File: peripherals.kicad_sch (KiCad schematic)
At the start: 81 parts, among them J10 533980471, J11 ERF8-040-05.0-L-DV-K-TR, J7 Conn_02x08_Counter_Clockwise, J9 TC2050-IDC-NL, Q10 PJE138K, Q9 PJE138K, U30 TPD4E05U06QDQARQ1, U33 NTS0102GT, U34 PCAL6408ABSHP

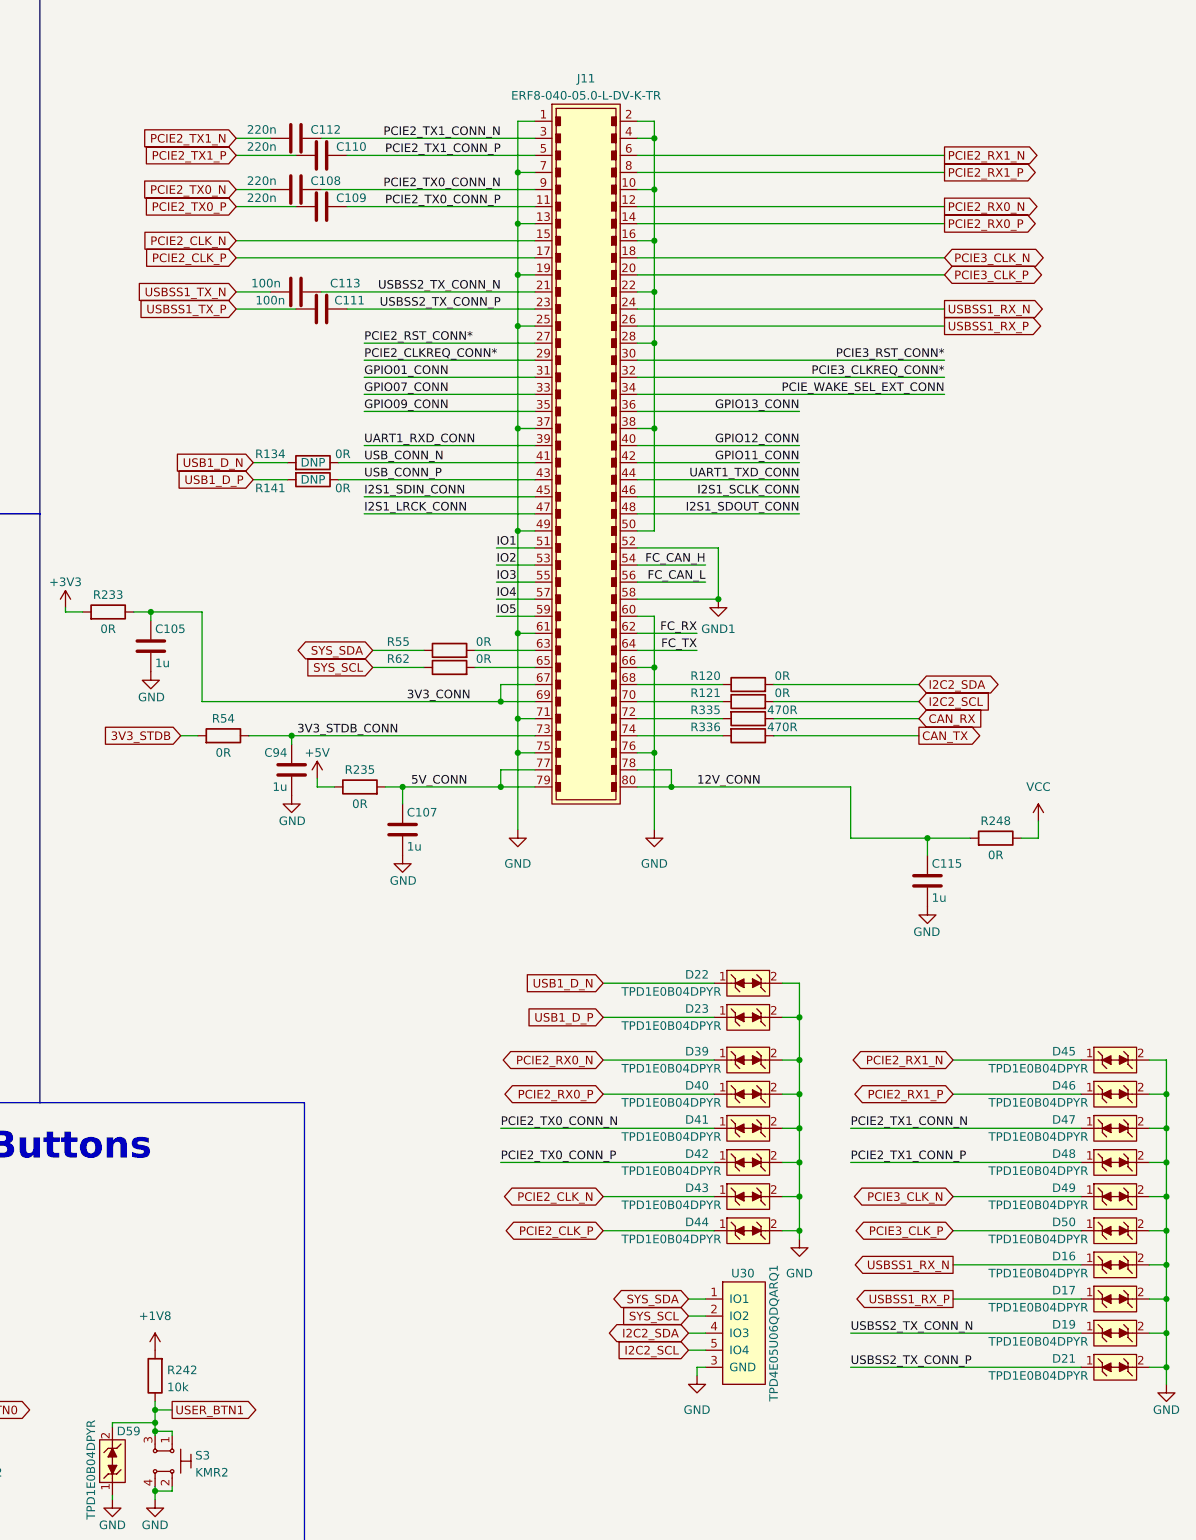
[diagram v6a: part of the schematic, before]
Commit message: Réduction des pins pour le payload
Voici ce que j'ai conservé:
-6 IO
-Communication CAN du skymate
-Mémoire flash pour serial (SYS_SDA/SYS_SCL)
-Communication serial (I2C2)
-Alimentation 3V3 5V 12V
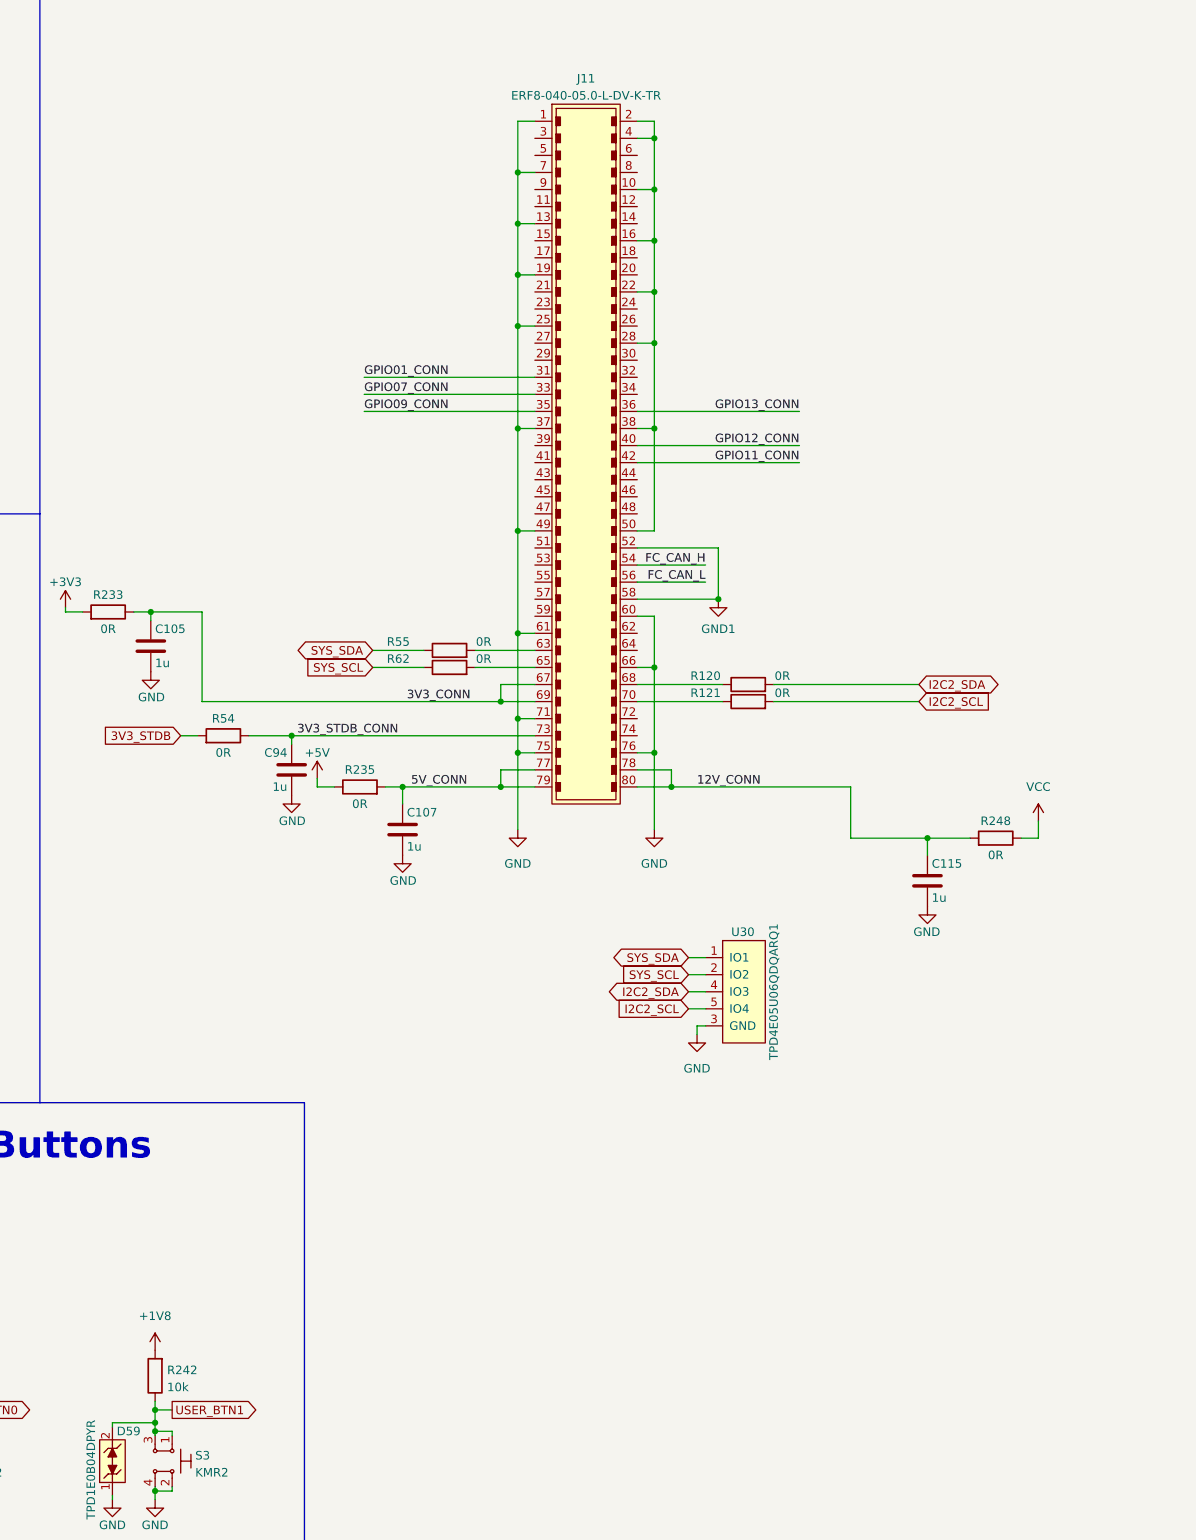
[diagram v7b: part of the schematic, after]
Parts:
- removed C108, C109, C110, C112: C_220n_0402, jetson-orin-baseboard-footprints:0402-cap, symbol jetson-orin-baseboard:C_220n_0402
- removed C111, C113: C_100n_0402, jetson-orin-baseboard-footprints:0402-cap, symbol jetson-orin-baseboard:C_100n_0402
- removed D16, D17, D19, D21, D22, D23, D39, D40, D41, D42, D43, D44, D45, D46, D47, D48, D49, D50: TPD1E0B04DPYR, jetson-orin-baseboard-footprints:XDFN-2_1x0.60mm, symbol jetson-orin-baseboard:TPD1E0B04DPYR
- removed R134, R141: R_0R_0402, jetson-orin-baseboard-footprints:0402-res, symbol jetson-orin-baseboard:R_0R_0402
- removed R335, R336: R_470R_0402, jetson-orin-baseboard-footprints:0402-res, symbol jetson-orin-baseboard:R_470R_0402
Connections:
- net FC_RX: no longer J11.62
- net FC_TX: no longer J11.64
- net I2S1_LRCK_CONN: no longer J11.47
- net I2S1_SCLK_CONN: no longer J11.46
- net I2S1_SDIN_CONN: no longer J11.45
- net I2S1_SDOUT_CONN: no longer J11.48
- net IO1: no longer J11.51
- net IO2: no longer J11.53
- net IO3: no longer J11.55
- net IO4: no longer J11.57
- net IO5: no longer J11.59
- net PCIE2_CLKREQ_CONN*: no longer J11.29
- net PCIE2_RST_CONN*: no longer J11.27
- net PCIE3_CLKREQ_CONN*: no longer J11.32
- net PCIE3_RST_CONN*: no longer J11.30
- net PCIE_WAKE_SEL_EXT_CONN: no longer J11.34
- net UART1_RXD_CONN: no longer J11.39
- net UART1_TXD_CONN: no longer J11.44
- net PCIE2_CLK_N: no longer names the net of J11.15
- net PCIE2_CLK_P: no longer names the net of J11.17
- net PCIE2_RX0_N: no longer names the net of J11.12
- net PCIE2_RX0_P: no longer names the net of J11.14
- net PCIE2_RX1_N: no longer names the net of J11.6
- net PCIE2_RX1_P: no longer names the net of J11.8
- net PCIE2_TX0_CONN_N: no longer names the net of J11.9
- net PCIE2_TX0_CONN_P: no longer names the net of J11.11
- net PCIE2_TX1_CONN_N: no longer names the net of J11.3
- net PCIE2_TX1_CONN_P: no longer names the net of J11.5
- net PCIE3_CLK_N: no longer names the net of J11.18
- net PCIE3_CLK_P: no longer names the net of J11.20
- net USBSS1_RX_N: no longer names the net of J11.24
- net USBSS1_RX_P: no longer names the net of J11.26
- net USBSS2_TX_CONN_N: no longer names the net of J11.21
- net USBSS2_TX_CONN_P: no longer names the net of J11.23
- net USB_CONN_N: no longer names the net of J11.41
- net USB_CONN_P: no longer names the net of J11.43
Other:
- moved on the sheet: U30

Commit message: changement vers gmsl2 en cours
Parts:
- J7: value Conn_02x08_Counter_Clockwise -> FC Conn
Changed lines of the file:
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@@
       (effects (font (size 1.27 1.27)))
     )
-    (property "Value" "Conn_02x08_Counter_Clockwise" (at 184.785 60.96 0)
+    (property "Value" "FC Conn" (at 184.785 60.96 0)
       (effects (font (size 1.27 1.27)))
     )
